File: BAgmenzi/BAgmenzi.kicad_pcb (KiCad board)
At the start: 2 copper layers, 11 parts, among them U1 OPA836IDBVT, U2 AD8338ACPZ-R7, U3 TPS22916CYFPR, U4 TPS22916CYFPR, U5 OPA836IDBVT, U6 LT3463AEDD#PBF, U7 MSP430FR5043IRGCT, X1 FY0800018, Y1 AWSCR-8.00CV-T

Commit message: added libraries, other changes in sch, started pcb
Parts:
- removed U5: OPA836IDBVT, wulpus:DBV0006A_L
- removed U6: LT3463AEDD#PBF, PCB1:LT-DD-10_V
- added C19: 2.2u, Capacitor_SMD:C_0402_1005Metric, F.Cu at (53.3, 111.6)
- added C20: 0.1u, Capacitor_SMD:C_0402_1005Metric, F.Cu at (54.3, 111.7)
- added C21: 2.2u, Capacitor_SMD:C_0402_1005Metric, F.Cu at (71.1, 112.1)
- added C22: 0.1u, Capacitor_SMD:C_0402_1005Metric, F.Cu at (71.1, 113.1)
- added C23: 2.2u, Capacitor_SMD:C_0402_1005Metric, F.Cu at (29.4, 116.6)
- added C24: 0.1u, Capacitor_SMD:C_0402_1005Metric, F.Cu at (29.4, 117.6)
- added C25: 10nF, Capacitor_SMD:C_0402_1005Metric, F.Cu at (30.1, 113.5)
- added C26: 1.5p, Capacitor_SMD:C_0402_1005Metric, F.Cu at (32.1, 114.5)
- added C27: 1n, Capacitor_SMD:C_0402_1005Metric, F.Cu at (50.9, 115.3)
- added C28: 10nF 100V, Capacitor_SMD:C_0402_1005Metric, F.Cu at (37.3, 115.7)
- added C29: 100p, Capacitor_SMD:C_0402_1005Metric, F.Cu at (71.1, 116.1)
- added C30: 1n, Capacitor_SMD:C_0402_1005Metric, F.Cu at (51.0, 113.8)
- added C31: 2.2u, Capacitor_SMD:C_0402_1005Metric, F.Cu at (34.1, 113.5)
- added C34: 1n, Capacitor_SMD:C_0402_1005Metric, F.Cu at (53.2, 117.0)
- added C35: 2.2u 50V, Capacitor_SMD:C_0402_1005Metric, F.Cu at (235.9, 72.6)
- added C36: 2.2u 50V, Capacitor_SMD:C_0402_1005Metric, F.Cu at (231.9, 72.8)
- added C37: 2.2u 50V, Capacitor_SMD:C_0402_1005Metric, F.Cu at (251.3, 109.3)
- added C38: 2.2u 50V, Capacitor_SMD:C_0402_1005Metric, F.Cu at (253.1, 109.3)
- added C39: 1u, Capacitor_SMD:C_0402_1005Metric, F.Cu at (241.0, 105.8)
- added C40: 2.2u 50V, Capacitor_SMD:C_0201_0603Metric, F.Cu at (243.6, 103.8)
- added C41: 2.2u 50V, Capacitor_SMD:C_0402_1005Metric, F.Cu at (244.8, 101.1)
- added C42: 2.2u 50V, Capacitor_SMD:C_0402_1005Metric, F.Cu at (244.8, 99.9)
- added C43: 2.2u 50V, Capacitor_SMD:C_0402_1005Metric, F.Cu at (249.3, 108.0)
- added C47: 22u, Capacitor_SMD:C_0402_1005Metric, F.Cu at (90.2, 40.6)
- added C48: 4.7u, Capacitor_SMD:C_0402_1005Metric, F.Cu at (86.1, 41.7)
- added C49: 1u, Capacitor_SMD:C_0402_1005Metric, F.Cu at (90.2, 39.6)
- added C50: 4.7u, Capacitor_SMD:C_0402_1005Metric, F.Cu at (84.9, 41.7)
- added C51: 1u, Capacitor_SMD:C_0402_1005Metric, F.Cu at (83.7, 39.2)
- added C52: 22u, Capacitor_SMD:C_0402_1005Metric, F.Cu at (87.1, 41.7)
- added C53: 3.3n, Capacitor_SMD:C_0402_1005Metric, F.Cu at (90.1, 38.7)
- added C54: 22u, Capacitor_SMD:C_0402_1005Metric, F.Cu at (88.4, 41.7)
- added C55: 0.1u, Capacitor_SMD:C_0402_1005Metric, F.Cu at (116.0, 36.0)
- added C56: 10u, Capacitor_SMD:C_0402_1005Metric, F.Cu at (81.5, 62.7)
- added C57: 22u, Capacitor_SMD:C_0402_1005Metric, F.Cu at (81.9, 66.4)
- added C58: 1u, Capacitor_SMD:C_0402_1005Metric, F.Cu at (81.9, 67.5)
- added C59: 1u, Capacitor_SMD:C_0402_1005Metric, F.Cu at (82.2, 71.6)
- added C60: 10u 10V, Capacitor_SMD:C_0402_1005Metric, F.Cu at (84.0, 75.1)
- added C63: 2.2U 50v, Capacitor_SMD:C_0201_0603Metric, F.Cu at (109.1, 125.1)
- added D1: APHD1608LZGCK, wulpus:FP-APHD1608LZGCK-MFG, F.Cu at (146.8, 71.1)
- added D3: NSR0340HT1G, Diode_SMD:D_SOD-323, F.Cu at (143.7, 58.6)
- added FB1: FerriteBead, Inductor_SMD:L_0603_1608Metric, F.Cu at (252.2, 107.6)
- added FB2: FerriteBead, Inductor_SMD:L_0603_1608Metric, F.Cu at (243.0, 100.5)
- added FB3: FerriteBead, PCB1:FP-BLM18-0_15-t0_8-IPC_A, F.Cu at (83.3, 73.3)
- added IC1: TPL0501-100RSER, KiCad:RSE0008A, F.Cu at (52.6, 118.7)
- added J2: DF52-2S-0.8H(21), wulpus:DF522S08H21, F.Cu at (112.8, 19.1)
- added J3: USB3076-30-A, EEG_PcbLib:CONN_USB3076-30-A_GCT, F.Cu at (135.0, 20.5)
- added L5: LQG15HS3N9B02D, wulpus:INDC1005X45N, F.Cu at (241.9, 104.7)
- added L6: LQG15HS3N9B02D, wulpus:INDC1005X45N, F.Cu at (242.0, 107.0)
- added L7: 1.5µH, EEG_PcbLib:IND_0805_DFE201210S, F.Cu at (90.3, 37.4)
- added L8: 2.2uH, Inductor_SMD:L_Murata_DFE201610P, F.Cu at (82.5, 64.5)
- added M1: *, AN54LM-20_PCB-260723:AN54LM-20_P20, F.Cu at (177.2, 37.4)
- added Q1: NX7002BKMBYL, wulpus_pro_acq:NX7002BKMBYL, F.Cu at (136.5, 94.0)
- added R10: 100, Resistor_SMD:R_0402_1005Metric, F.Cu at (35.1, 115.7)
- added R11: 400, Resistor_SMD:R_0402_1005Metric, F.Cu at (55.1, 117.0)
- added R11oderC_direct1: 0Ohm, oder 10nF 100V, Resistor_SMD:R_0402_1005Metric, F.Cu at (246.6, 75.0)
- added R12: 47k, Resistor_SMD:R_0402_1005Metric, F.Cu at (34.1, 114.5)
- added R13: 10k, Resistor_SMD:R_0402_1005Metric, F.Cu at (91.3, 107.4)
- added R15: 1.3k, Resistor_SMD:R_0402_1005Metric, F.Cu at (54.9, 118.8)
- added R16: 2.7k, Resistor_SMD:R_0402_1005Metric, F.Cu at (51.3, 117.0)
- added R17: 51, Resistor_SMD:R_0402_1005Metric, F.Cu at (132.4, 89.5)
- added R18: 1OK, Resistor_SMD:R_0402_1005Metric, F.Cu at (127.5, 90.2)
- added R19: 10K, Resistor_SMD:R_0402_1005Metric, F.Cu at (127.5, 92.0)
- added R20: 1M, Resistor_SMD:R_0402_1005Metric, F.Cu at (245.3, 102.7)
- added R21: 43.2k, Resistor_SMD:R_0402_1005Metric, F.Cu at (245.3, 103.7)
- added R22: 41.2k, Resistor_SMD:R_0402_1005Metric, F.Cu at (247.8, 106.5)
- added R23: 1M, Resistor_SMD:R_0402_1005Metric, F.Cu at (247.8, 107.5)
- added R24: 10k, Resistor_SMD:R_0402_1005Metric, F.Cu at (243.1, 108.9)
- added R25: 10k, Resistor_SMD:R_0402_1005Metric, F.Cu at (244.1, 108.9)
- added R32: 4.7k, Resistor_SMD:R_0402_1005Metric, F.Cu at (87.8, 36.1)
- added R33: 4.7k, Resistor_SMD:R_0402_1005Metric, F.Cu at (85.1, 36.2)
- added R34: 100k, Resistor_SMD:R_0402_1005Metric, F.Cu at (86.7, 36.1)
- added R35: 100k, Resistor_SMD:R_0402_1005Metric, F.Cu at (84.0, 36.1)
- added R36: 10K, Resistor_SMD:R_0402_1005Metric, F.Cu at (80.4, 41.1)
- added R37: 100k, Resistor_SMD:R_0402_1005Metric, F.Cu at (75.8, 63.6)
- added R38: 20.5k, Resistor_SMD:R_0402_1005Metric, F.Cu at (77.3, 67.1)
- added R39: 0, Resistor_SMD:R_0402_1005Metric, F.Cu at (76.0, 67.1)
- added R40: 0, Resistor_SMD:R_0402_1005Metric, F.Cu at (74.6, 67.1)
- added R7: 2k, Resistor_SMD:R_0402_1005Metric, F.Cu at (30.1, 114.5)
- added R8: 2k, Resistor_SMD:R_0402_1005Metric, F.Cu at (32.1, 113.5)
- added R9: 400, Resistor_SMD:R_0402_1005Metric, F.Cu at (71.1, 115.2)
- added RT1: 10k at 25°C, Resistor_SMD:R_0402_1005Metric, F.Cu at (80.4, 42.3)
- added S1: NanoT160BP, wulpus:NanoT160BP, F.Cu at (84.5, 30.9)
- added TP2: vga_vref, TestPoint:TestPoint_Loop_D2.50mm_Drill1.85mm, F.Cu at (54.7, 138.7)
- added TP6: TestPoint, TestPoint:TestPoint_Loop_D2.50mm_Drill1.0mm_LowProfile, F.Cu at (58.0, 132.7)
- added TP7: +V_hv_in, EEG_PcbLib:TEST_POINT_KEYSTONE_5007_TRAD, F.Cu at (235.5, 91.7)
- added U10: PESD1USB30, EEG_PcbLib:WLCSP_5_2-1-2_P0.4, F.Cu at (124.8, 23.5)
- added U11: MAX77654BENV+T, EEG_PcbLib:WLP_30_MAX77654, F.Cu at (85.8, 38.0)
- added U12: TS5A3159AYZPR, wulpus_pro_acq:BGA6C50P2X3_89X139X50, F.Cu at (114.0, 36.0)
- added U13: TPS7A20xxxDQN, Package_SON:Texas_X2SON-4_1x1mm_P0.65mm, F.Cu at (82.1, 69.9)
- added U14: TPS63900, Package_SON:WSON-10-1EP_2.5x2.5mm_P0.5mm_EP1.2x2mm_ThermalVias, F.Cu at (79.1, 64.6)
- added U8: TPS22916CYFPR, BGA4C40P2X2_78X78X50:BGA4C40P2X2_78X78X50, F.Cu at (161.1, 61.2)
- added U9: MAXM86161EFD_T, MAXM86161EFD_T:PSON60P430X290X150-14N, F.Cu at (147.1, 65.0)
- D2: value APHD1608LZGCK -> ZHCS400QTA; footprint wulpus:FP-APHD1608LZGCK-MFG -> Diode_SMD:D_SOD-323_HandSoldering
- U1: value OPA836IDBVT -> MSP430FR5043IRGCT; footprint wulpus:DBV0006A_L -> wulpus:RGC0064G
- U3, U4: value TPS22916CYFPR -> OPA836IDBVT; footprint BGA4C40P2X2_78X78X50:BGA4C40P2X2_78X78X50 -> wulpus:DBV0006A_L
- U7: value MSP430FR5043IRGCT -> LT3463AEDD#PBF; footprint wulpus:RGC0064G -> PCB1:LT-DD-10_V
- moved U2 112.3 mm to (53.9, 114.5)
- moved U7 93.7 mm to (244.9, 105.9)
- moved D2 87.5 mm to (246.8, 109.0)
- moved B1 80.5 mm to (234.0, 75.5)
- moved U3 67.2 mm to (32.2, 116.6), turned to 180 degrees
- moved U4 33.2 mm to (68.3, 114.1)
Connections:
- net /TX/+HV renamed +HV
- D2 pad 1: unconnected-(D2-C-Pad1) -> HV_NEG_EN
- D2 pad 2: /MSP/LED_MSP430 -> /TX/VOUT_NEG
- U1 pad 1: /RX/VGA_IN -> /MSP/AVCC1
- U1 pad 2: GND -> VGA_GAIN_RC_SINK
- U1 pad 3: Net-(U1-VIN+) -> VGA_GAIN_RC_EN
- U1 pad 4: Net-(U1-VIN-) -> VGA_GAIN_CS
- U1 pad 5: /RX/PREAMP_SHDN_N -> GND
- U1 pad 6: /RX/+V_PREAMP -> /MSP/LFXIN
- U2 pad 1: unconnected-(U2-INPR-Pad1) -> Net-(U2-INPR)
- U2 pad 13: GND -> /RX/VGA_REF
- U2 pad 15: /RX/+V_VGA -> V_RX
- U2 pad 16: GND -> /RX/VGA_REF
- U2 pad 2: Net-(U2-INPD) -> unconnected-(U2-INPD-Pad2)
- U2 pad 6: /RX/+V_VGA -> V_RX
- U7 pad 1: /MSP/AVCC1 -> /TX/VOUT_POS
- U7 pad 10: /MSP/HFXOUT -> Net-(U7-FB1)
- U7 pad 11: /MSP/JTAG_TEST -> GND
- U7 pad 2: VGA_GAIN_RC_SINK -> Net-(U7-SW1)
- U7 pad 3: VGA_GAIN_RC_EN -> /TX/+V_IN_HV
- U7 pad 4: VGA_GAIN_CS -> HV_NEG_EN
- U7 pad 5: GND -> HV_NEG_EN
- U7 pad 6: /MSP/LFXIN -> Net-(U7-FB2)
- U7 pad 7: /MSP/LFXOUT -> Net-(U7-VREF)
- U7 pad 8: GND -> HV_NEG_EN
- U7 pad 9: /MSP/HFXIN -> HV_NEG_EN
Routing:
- net GND: track 0.00 -> 11.1 mm, vias 0 -> 18
- net /TX/PULSER_OUT: track 0.00 -> 11.0 mm
- net +HV: track 0.00 -> 7.05 mm
- net /RX/VGA_IN: track 0.00 -> 5.69 mm, vias 0 -> 1
- net Net-(U3-VIN-): track 0.00 -> 3.27 mm
- net Net-(U3-VIN+): track 0.00 -> 2.30 mm
- net Net-(C28-Pad2): track 0.00 -> 1.22 mm
- net (no net): track 0.00 -> 1.07 mm
- net V_RX: track 0.00 -> 1.06 mm
- net Net-(C25-Pad2): track 0.00 -> 1.04 mm
- net /RX/VGA_REF: track 0.00 -> 1.01 mm
- net HV_NEG_EN: track 0.00 -> 0.57 mm
- net Net-(U7-FB2): track 0.00 -> 0.56 mm
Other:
- copper layers 2 -> 6

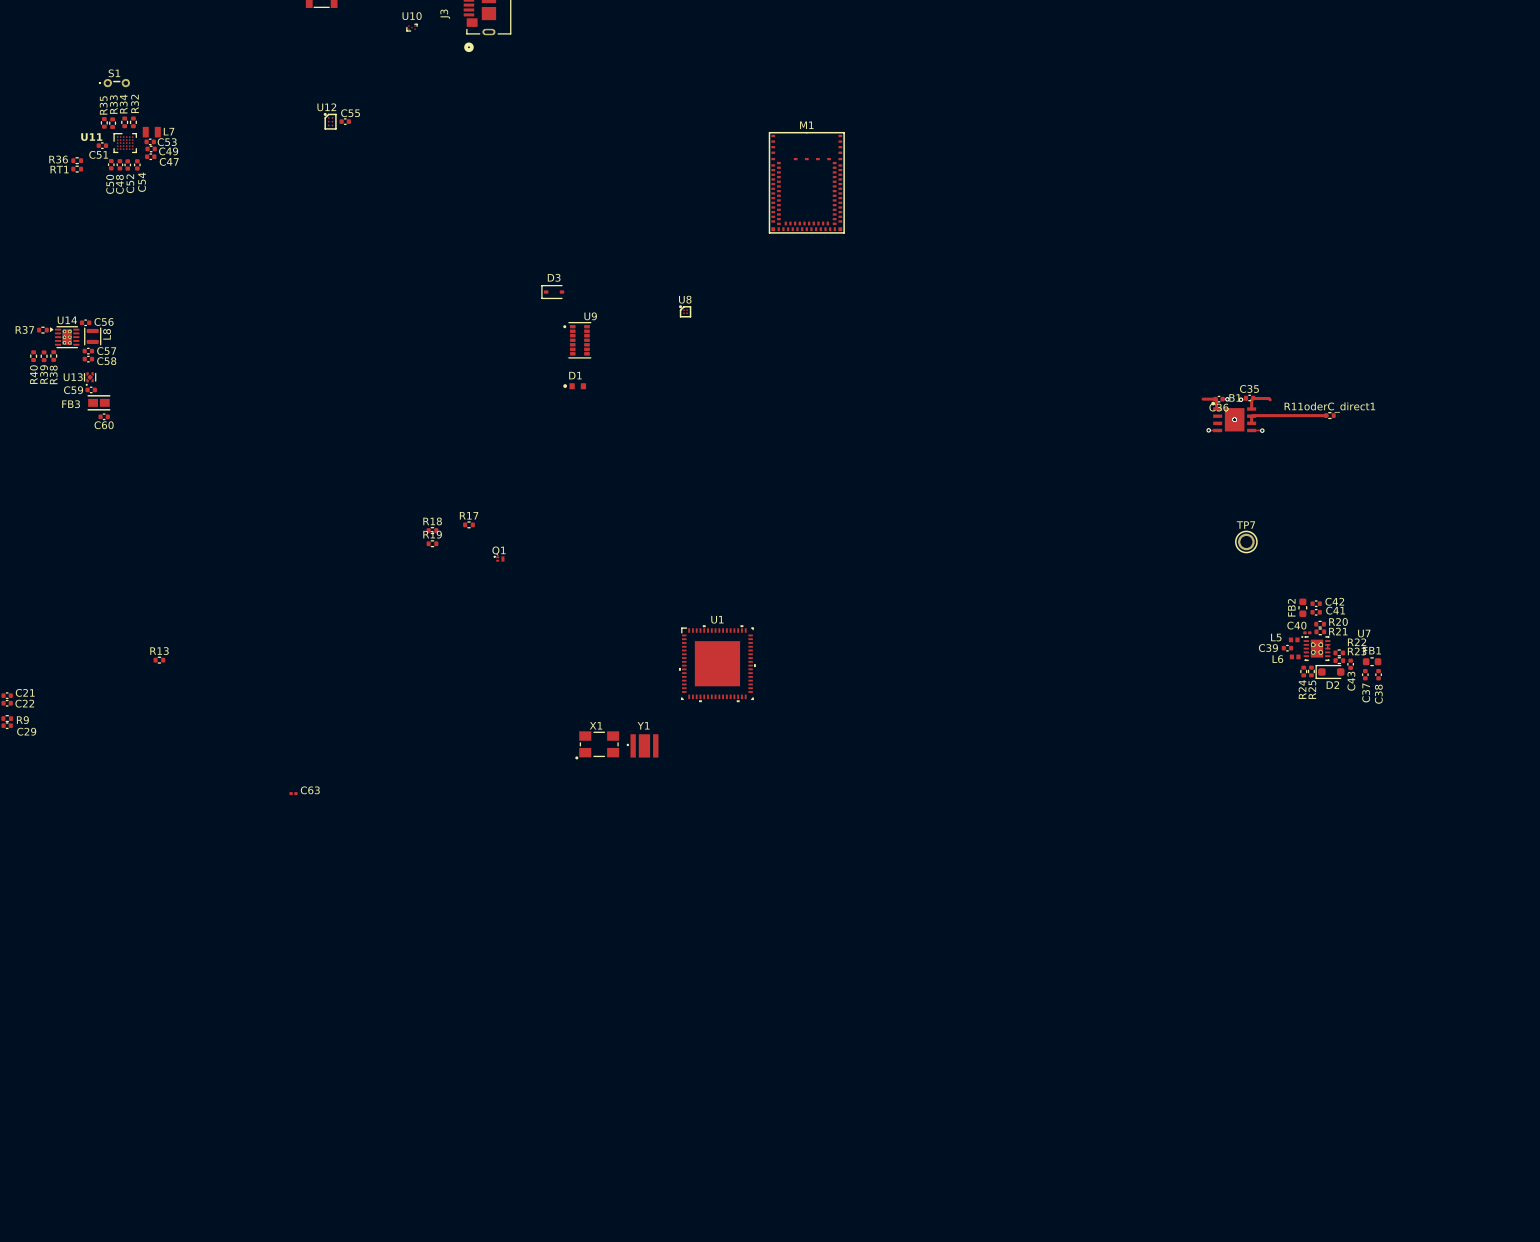
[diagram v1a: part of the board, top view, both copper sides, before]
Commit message: changed VRX rail and deleted U12
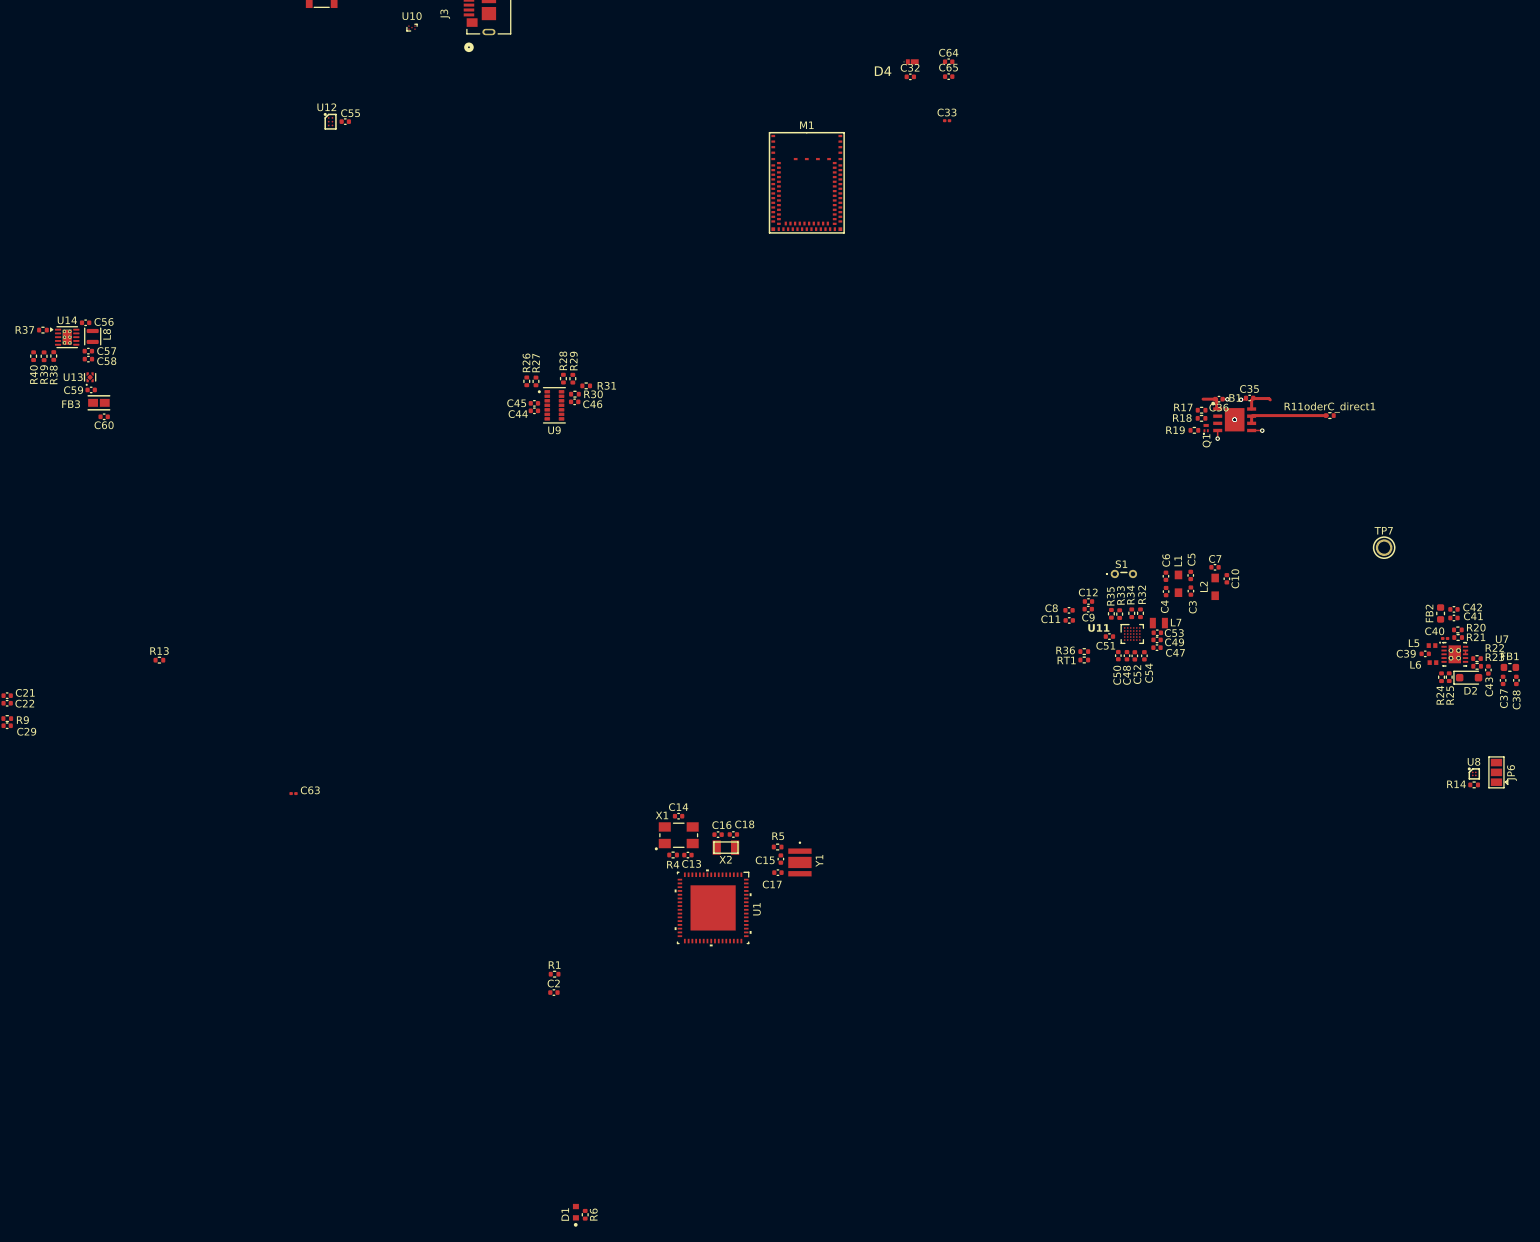
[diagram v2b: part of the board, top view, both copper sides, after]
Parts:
- removed D3: NSR0340HT1G, Diode_SMD:D_SOD-323
- added C10: 0.1u, Capacitor_SMD:C_0402_1005Metric, F.Cu at (232.9, 96.6)
- added C11: 0.1u, Capacitor_SMD:C_0402_1005Metric, F.Cu at (212.0, 102.2)
- added C12: 0.1u, Capacitor_SMD:C_0402_1005Metric, F.Cu at (214.6, 99.6)
- added C13: 12p, Capacitor_SMD:C_0402_1005Metric, F.Cu at (161.4, 133.3)
- added C14: 12p, Capacitor_SMD:C_0402_1005Metric, F.Cu at (160.2, 128.1)
- added C15: 12p, Capacitor_SMD:C_0402_1005Metric, F.Cu at (173.8, 133.8)
- added C16: 12p, Capacitor_SMD:C_0402_1005Metric, F.Cu at (165.4, 130.6)
- added C17: 12p, Capacitor_SMD:C_0402_1005Metric, F.Cu at (173.4, 135.6)
- added C18: 12p, Capacitor_SMD:C_0402_1005Metric, F.Cu at (167.4, 130.5)
- added C2: 1n, Capacitor_SMD:C_0402_1005Metric, F.Cu at (143.6, 151.5)
- added C3: 47u, Capacitor_SMD:C_0402_1005Metric, F.Cu at (228.2, 98.3)
- added C32: 0.1u, Capacitor_SMD:C_0402_1005Metric, F.Cu at (190.9, 30.0)
- added C33: 0.1u 50V, Capacitor_SMD:C_0201_0603Metric, F.Cu at (195.8, 35.9)
- added C4: 47u, Capacitor_SMD:C_0402_1005Metric, F.Cu at (224.9, 98.3)
- added C44: 10u, Capacitor_SMD:C_0402_1005Metric, F.Cu at (141.1, 74.3)
- added C45: 1u, Capacitor_SMD:C_0402_1005Metric, F.Cu at (141.1, 73.3)
- added C46: 1u, Capacitor_SMD:C_0402_1005Metric, F.Cu at (146.4, 73.2)
- added C5: 1n, Capacitor_SMD:C_0402_1005Metric, F.Cu at (228.1, 96.2)
- added C6: 1n, Capacitor_SMD:C_0402_1005Metric, F.Cu at (224.8, 96.3)
- added C64: 4.7u, Capacitor_SMD:C_0402_1005Metric, F.Cu at (196.0, 28.0)
- added C65: 4.7u, Capacitor_SMD:C_0402_1005Metric, F.Cu at (196.0, 30.0)
- added C7: 2.2u, Capacitor_SMD:C_0402_1005Metric, F.Cu at (231.3, 95.1)
- added C8: 2.2u, Capacitor_SMD:C_0402_1005Metric, F.Cu at (212.0, 100.8)
- added C9: 2.2u, Capacitor_SMD:C_0402_1005Metric, F.Cu at (214.5, 100.7)
- added D4: NSR20F30NXT5G, NSR20F30NXT5G:DSN2_1, F.Cu at (191.2, 28.0)
- added JP6: SolderJumper_3_Open, Jumper:SolderJumper-3_P1.3mm_Open_Pad1.0x1.5mm, F.Cu at (268.7, 122.3)
- added L1: 600Ohm, wulpus:SMD-0805, F.Cu at (226.5, 97.3)
- added L2: 600Ohm, wulpus:SMD-0805, F.Cu at (231.4, 97.7)
- added R1: 47k, Resistor_SMD:R_0402_1005Metric, F.Cu at (143.7, 149.1)
- added R14: 100k, Resistor_SMD:R_0402_1005Metric, F.Cu at (265.7, 124.0)
- added R26: 4.7k, Resistor_SMD:R_0402_1005Metric, F.Cu at (140.0, 70.4)
- added R27: 4.7k, Resistor_SMD:R_0402_1005Metric, F.Cu at (141.3, 70.4)
- added R28: 47k, Resistor_SMD:R_0402_1005Metric, F.Cu at (144.9, 70.1)
- added R29: 47k, Resistor_SMD:R_0402_1005Metric, F.Cu at (146.2, 70.1)
- added R30: 1k, Resistor_SMD:R_0402_1005Metric, F.Cu at (146.4, 72.1)
- added R31: DNP, Resistor_SMD:R_0402_1005Metric, F.Cu at (147.9, 71.0)
- added R4: 22, Resistor_SMD:R_0402_1005Metric, F.Cu at (159.4, 133.3)
- added R5: 22, Resistor_SMD:R_0402_1005Metric, F.Cu at (173.3, 132.2)
- added R6: 22, Resistor_SMD:R_0402_1005Metric, F.Cu at (147.8, 181.0)
- added X2: ABS07-32.768KHZ-9-T, PcbLib1:XTAL320X150X90, F.Cu at (166.5, 132.3)
- J2: footprint wulpus:DF522S08H21 -> SamacSys:DF522S08H21
- U13: value TPS7A20xxxDQN -> TPS7A2033DBVDQN
- Y1: footprint wulpus:AWSCR-8.00CV-T_ABR -> PcbLib1:AWSCR-8.00CV-T_ABR
- moved C50 148.6 mm to (218.5, 106.8)
- moved C51 148.6 mm to (217.3, 104.3)
- moved C52 148.6 mm to (220.7, 106.8)
- moved C53 148.6 mm to (223.7, 103.8)
- moved L7 148.6 mm to (223.9, 102.5)
- moved R32 148.6 mm to (221.5, 101.2)
- moved R34 148.6 mm to (220.3, 101.2)
- moved R35 148.6 mm to (217.6, 101.3)
- moved R36 148.6 mm to (214.0, 106.3)
- moved RT1 148.6 mm to (214.0, 107.4)
- moved S1 148.6 mm to (218.1, 96.0)
- moved U11 148.6 mm to (219.4, 103.2)
- moved C48 148.6 mm to (219.7, 106.8)
- moved C54 148.6 mm to (222.0, 106.8)
- moved R33 148.6 mm to (218.7, 101.3)
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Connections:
- net /CMUT/PULSE_HV_IN renamed PULSE_HV
- net /CMUT/RX_OUT renamed RX_IN
- net /MSP/JTAG_TEST renamed JTAG.TEST
- net /POWER/V_SYS renamed V_SYS
- net /RX/RX_PATH_SPI.CLK renamed VGA_SPI.SCLK
- net /RX/SIG_FILT_IN renamed SIG_FILT_IN
- net PWR.V_BAT renamed V_BAT
- net USB_BUS.VUSB renamed CHGIN
- net VGA_SPI.CLK renamed /MSP/VGA_SPI.CLK
- C47 pad 1: /POWER/DVDD_3.3 -> DVDD_3.3
- C54 pad 1: /POWER/V_LED -> V_LED
- D1 pad 1: unconnected-(D1-C-Pad1) -> Net-(D1-C)
- D2 pad 1: HV_NEG_EN -> Net-(D2-K)
- IC1 pad 3: /RX/VGA_GAIN_CS -> VGA_GAIN_CS
- J3 pad 4: unconnected-(J3-Pad4) -> GND
- J3 pad 5: unconnected-(J3-Pad5) -> GND
- L6 pad 2: HV_NEG_EN -> Net-(U7-SW2)
- M1 pad 1: unconnected-(M1-GND-Pad1) -> GND
- M1 pad 13: unconnected-(M1-D--Pad13) -> USB.D_N
- M1 pad 14: unconnected-(M1-GND-Pad14) -> GND
- M1 pad 15: unconnected-(M1-D+-Pad15) -> USB.D_P
- M1 pad 2: unconnected-(M1-GND-Pad2) -> GND
- M1 pad 25: unconnected-(M1-GND-Pad25) -> GND
- M1 pad 27: unconnected-(M1-VBUS_NRF-Pad27) -> USB.VUSB
- M1 pad 29: unconnected-(M1-GND-Pad29) -> GND
- M1 pad 3: unconnected-(M1-NRESET-Pad3) -> soft_RST
- M1 pad 4: unconnected-(M1-P0.07-Pad4) -> PMIC_I2C.SCL
- M1 pad 42: unconnected-(M1-P2.05-Pad42) -> NRF_MSP_CS
- M1 pad 47: unconnected-(M1-P2.06-Pad47) -> LINK_READY
- M1 pad 48: unconnected-(M1-P2.04-Pad48) -> NRF_SPI.MISO
- M1 pad 5: unconnected-(M1-SWCLK-Pad5) -> SWCLK
- M1 pad 50: unconnected-(M1-P2.02-Pad50) -> NRF_SPI.MOSI
- M1 pad 51: unconnected-(M1-P2.01-Pad51) -> NRF_SPI.SCLK
- M1 pad 53: unconnected-(M1-GND-Pad53) -> GND
- M1 pad 54: unconnected-(M1-P1.05/AIN5-Pad54) -> PMIC_AMUX
- M1 pad 55: unconnected-(M1-P1.07/EXTREF-Pad55) -> PPG_I2C.SCL
- M1 pad 56: unconnected-(M1-P1.08-Pad56) -> PPG_I2C.SDA
- M1 pad 57: unconnected-(M1-P1.09-Pad57) -> PPG_INT
- M1 pad 6: unconnected-(M1-P0.05-Pad6) -> PMIC_IRQ
- M1 pad 69: unconnected-(M1-GND-Pad69) -> GND
- M1 pad 7: unconnected-(M1-SWDIO-Pad7) -> SWDIO
- M1 pad 70: unconnected-(M1-P1.10-Pad70) -> DATA_READY
- M1 pad 71: unconnected-(M1-VDD_NRF-Pad71) -> DVDD_3.3
- M1 pad 76: unconnected-(M1-P1.11-Pad76) -> UUPS_TRIG_IN
- M1 pad 77: unconnected-(M1-P1.12-Pad77) -> PPG_GPIO
- M1 pad 80: unconnected-(M1-P0.08-Pad80) -> PMIC_I2C.SDA
- M1 pad 81: unconnected-(M1-GND-Pad81) -> GND
- M1 pad 82: unconnected-(M1-GND-Pad82) -> GND
- M1 pad 83: unconnected-(M1-GND-Pad83) -> GND
- M1 pad 84: unconnected-(M1-GND-Pad84) -> GND
- M1 pad 85: unconnected-(M1-GND-Pad85) -> GND
- M1 pad 86: unconnected-(M1-GND-Pad86) -> GND
- M1 pad 87: unconnected-(M1-GND-Pad87) -> GND
- M1 pad 88: unconnected-(M1-GND-Pad88) -> GND
- M1 pad 89: unconnected-(M1-GND-Pad89) -> GND
- M1 pad 90: unconnected-(M1-GND-Pad90) -> GND
- M1 pad 91: unconnected-(M1-GND-Pad91) -> GND
- M1 pad 92: unconnected-(M1-GND-Pad92) -> GND
- M1 pad 93: unconnected-(M1-GND-Pad93) -> GND
- Q1 pad 1: /TX/PULSE_EN_N -> PULSER_HIZ_IN
- R13 pad 1: /RX/FILTER_SHDN_N -> LP_FILT_EN
- R15 pad 1: /RX/VGA_GAIN_RC_SINK -> VGA_GAIN_RC_SINK
- R16 pad 1: /RX/VGA_GAIN_RC_EN -> VGA_GAIN_RC_EN
- R17 pad 1: /TX/PULSE_LV_IN -> PULSE_OUT
- R19 pad 1: /TX/PULSE_EN_N -> PULSER_HIZ_IN
- R24 pad 1: HV_NEG_EN -> HV_POS_EN
- R32 pad 1: /POWER/DVDD_3.3 -> DVDD_3.3
- R33 pad 1: /POWER/DVDD_3.3 -> DVDD_3.3
- R34 pad 1: /POWER/DVDD_3.3 -> DVDD_3.3
- R34 pad 2: /POWER/IRQ -> PMIC_IRQ
- R35 pad 1: /POWER/DVDD_3.3 -> DVDD_3.3
- R35 pad 2: Net-(U11A-~{RST}) -> soft_RST
- TP6 pad 1: /RX/VGA_GAIN_RC_SINK -> VGA_GAIN_RC_SINK
- U1 pad 12: /MSP/JTAG_RESET_N -> JTAG.RESET_N
- U1 pad 18: /MSP/DVCC1 -> DVDD_3.3
- U1 pad 21: unconnected-(U1-P2.0_UCA1CLK_UCA3SIMO_UCA3TXD-Pad21) -> BSL.UART_TX
- U1 pad 22: unconnected-(U1-P2.1_UCA1STE_UCA3SOMI_UCA3RXD-Pad22) -> BSL.UART_RX
- U1 pad 24: /MSP/UUPS_TRIG_IN -> UUPS_TRIG_IN
- U1 pad 36: /MSP/NRF_SPI.CLK -> NRF_SPI.SCLK
- U1 pad 41: NRF_LINK_READY -> LINK_READY
- U1 pad 42: NRF_DATA_READY -> DATA_READY
- U1 pad 44: /MSP/UUPS_TRIG_IN -> unconnected-(U1-P6.5_SMCLK-Pad44)
- U1 pad 49: /MSP/DVCC3 -> DVDD_3.3
- U1 pad 50: HV_NEG_EN -> HV_POS_EN
- U1 pad 56: GND -> /MSP/PVCC
- U1 pad 57: GND -> /MSP/PVCC
- U1 pad 59: /MSP/CH0_OUT -> PULSE_OUT
- U10 pad C1: USB_BUS.D_P -> USB.D_P
- U10 pad C2: USB_BUS.D_N -> USB.D_N
- U11 pad A2: Net-(U11A-~{RST}) -> soft_RST
- U11 pad A4: /POWER/DVDD_3.3 -> DVDD_3.3
- U11 pad B2: /POWER/IRQ -> PMIC_IRQ
- U11 pad C1: /POWER/AMUX -> PMIC_AMUX
- U11 pad C4: /POWER/DVDD_3.3 -> DVDD_3.3
- U11 pad D4: /POWER/V_LED -> V_LED
- U12 pad A1: /POWER/soft_RST -> soft_RST
- U4 pad 5: /RX/FILTER_SHDN_N -> LP_FILT_EN
- U7 pad 4: HV_NEG_EN -> Net-(U7-SW2)
- U7 pad 5: HV_NEG_EN -> Net-(D2-K)
- U7 pad 9: HV_NEG_EN -> HV_POS_EN
- U9 pad 1: /PPG/PPG_I2C.SDA -> PPG_I2C.SDA
- U9 pad 13: /PPG/PPG_INT -> Net-(U9-GPIO)
- U9 pad 14: Net-(U9-INTB) -> PPG_INT
- U9 pad 2: /PPG/PPG_I2C.SCL -> PPG_I2C.SCL
- U9 pad 3: /PPG/VD_NRF -> DVDD_3.3
- U9 pad 5: /PPG/V_LED -> V_LED
